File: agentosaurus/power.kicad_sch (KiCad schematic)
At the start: 4 parts, among them J1 ATX_24Pin, U1 TPS54360DDA, U2 AMS1117-3.3

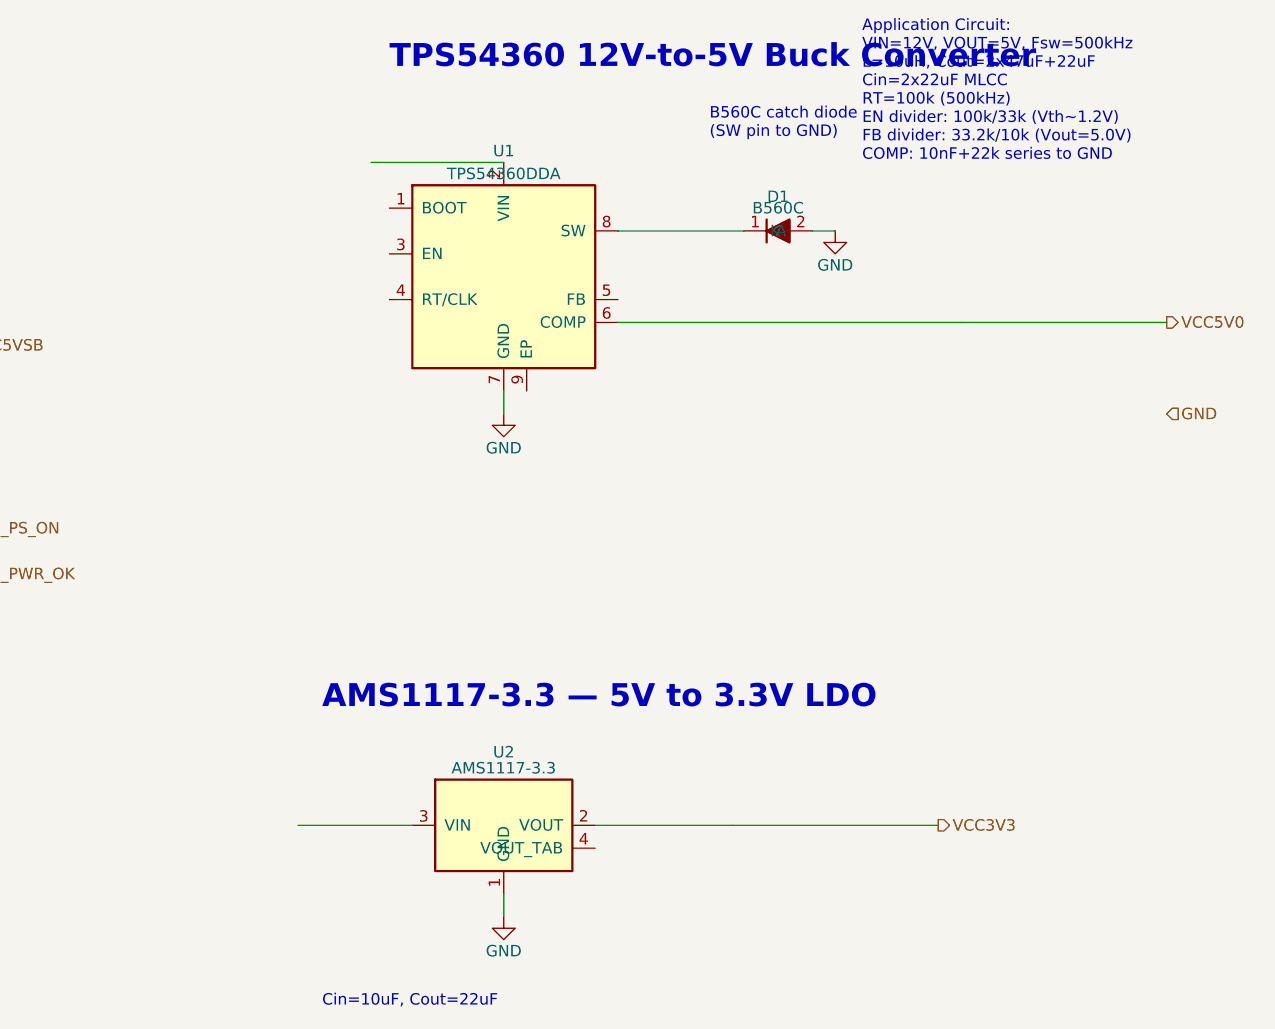
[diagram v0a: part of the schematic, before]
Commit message: Add passive components to all schematic sheets
- power.kicad_sch: Fix D1 catch diode rotation (cathode→SW), remove
  incorrect COMP-to-output wire, add all TPS54360 application circuit
  passives (CIN1/2, CBOOT, L1, COUT1-3, R_EN1/2, R_RT, R_FB1/2,
  R_COMP, C_COMP) and AMS1117 caps (CIN_LDO, COUT_LDO)
- bmc.kicad_sch: Add USB-C CC pull-downs (R1/R2 5.1k), ESP32 reset
  circuit (R3 10k + C9 1uF), decoupling caps for ESP32 (C10/C11),
  UART mux (C12), USB mux (C13/C14), WS2812B (C15-C18), I2C
  pull-ups (R4/R5 4.7k)
- cm4-slot.kicad_sch: Add magnetics center-tap decoupling (C1-C4
  100nF) and power rail decoupling (C5-C8)
- ethernet-switch.kicad_sch: Add crystal load caps (C1/C2 22pF),
  3.3V decoupling (C3-C10), 1.0V core decoupling (C11-C16),
  Slot 2 Ethernet wiring to RTL8367S
- mechanical.kicad_sch: Add PCB stackup, impedance control, and
  via specifications

https://claude.ai/code/session_01UhhXLgEHsAy83XEALyNrDb
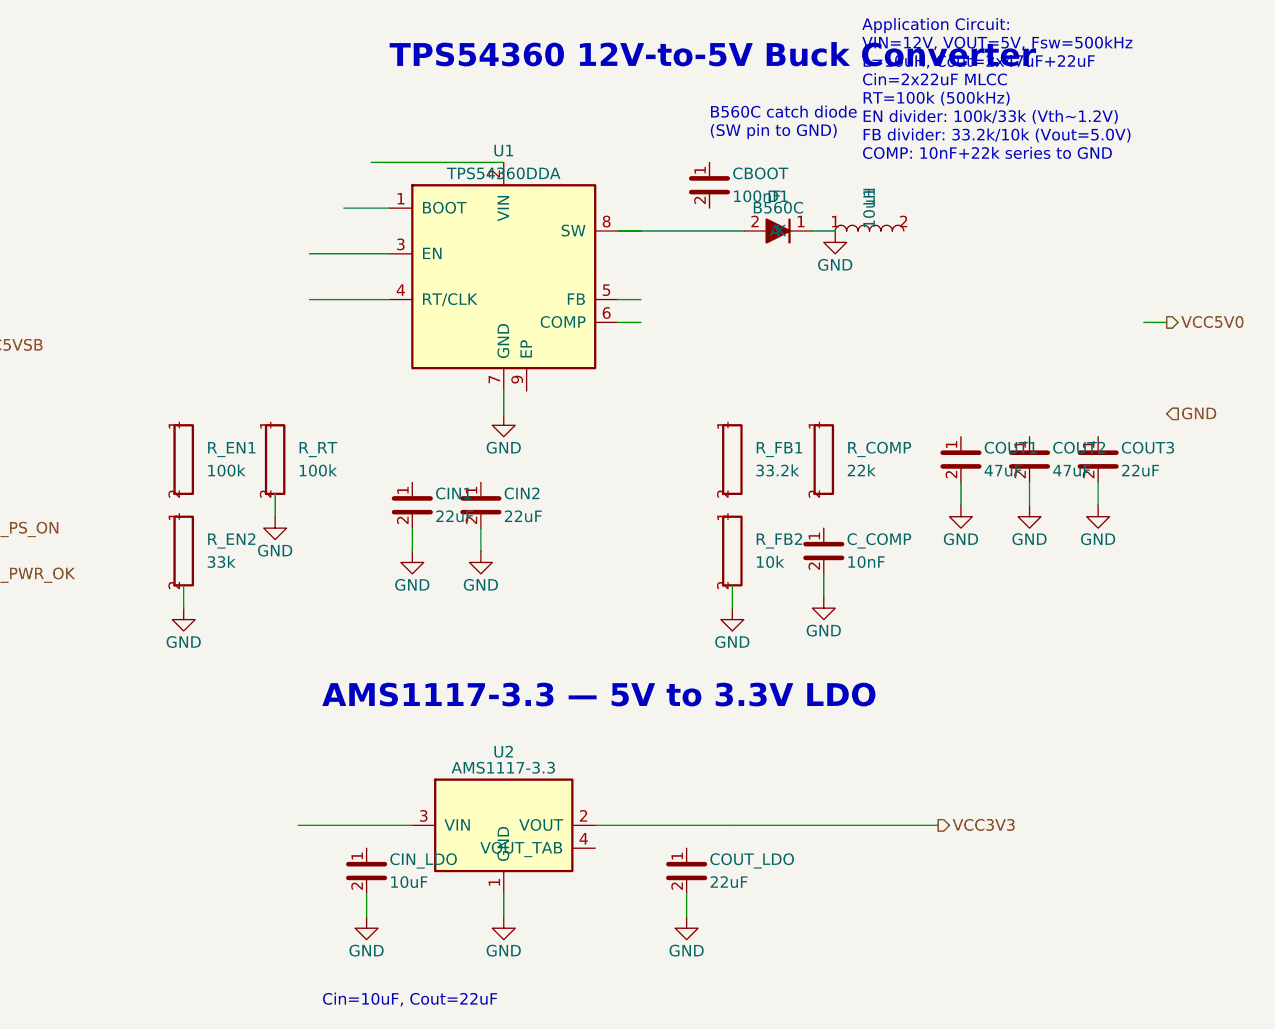
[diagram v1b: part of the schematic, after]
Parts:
- added CBOOT: 100nF, Capacitor_SMD:C_0402_1005Metric, symbol Device:C
- added CIN1, CIN2, COUT3, COUT_LDO: 22uF, Capacitor_SMD:C_0805_2012Metric, symbol Device:C
- added CIN_LDO: 10uF, Capacitor_SMD:C_0805_2012Metric, symbol Device:C
- added COUT1, COUT2: 47uF, Capacitor_SMD:C_0805_2012Metric, symbol Device:C
- added C_COMP: 10nF, Capacitor_SMD:C_0402_1005Metric, symbol Device:C
- added L1: 10uH, Inductor_SMD:L_1210_3225Metric, symbol Device:L
- added R_COMP: 22k, Resistor_SMD:R_0402_1005Metric, symbol Device:R
- added R_EN1, R_RT: 100k, Resistor_SMD:R_0402_1005Metric, symbol Device:R
- added R_EN2: 33k, Resistor_SMD:R_0402_1005Metric, symbol Device:R
- added R_FB1: 33.2k, Resistor_SMD:R_0402_1005Metric, symbol Device:R
- added R_FB2: 10k, Resistor_SMD:R_0402_1005Metric, symbol Device:R
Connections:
- net GND: now also D1.1 (A), CIN1.2, CIN2.2, CIN_LDO.2, COUT1.2, COUT2.2, COUT3.2, COUT_LDO.2, C_COMP.2, L1.1, R_EN2.2, R_FB2.2, R_RT.2; no longer D1.2 (K)
- net VCC5V0: no longer U1.6 (COMP)
- net at U1.8 (SW): now also D1.2 (K); no longer D1.1 (A)
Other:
- moved on the sheet: D1

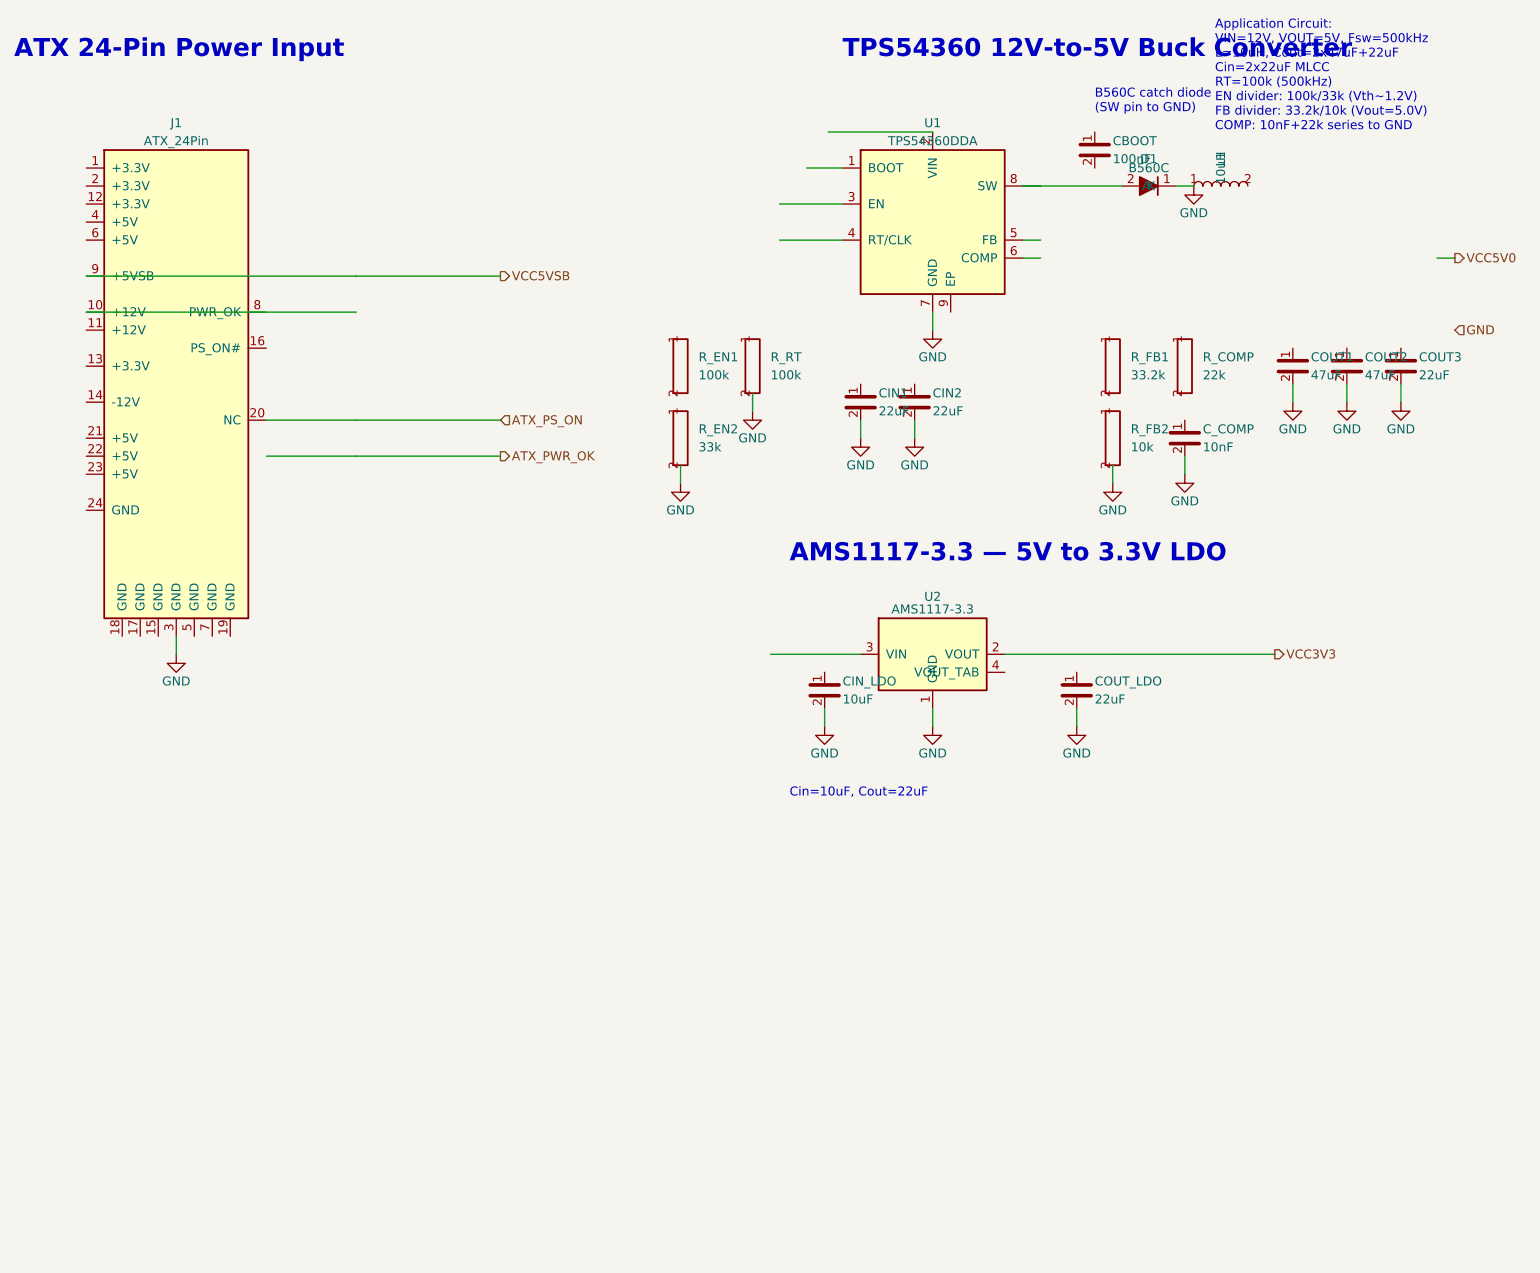
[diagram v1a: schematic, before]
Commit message: Clean up power sheet: reorganize passives and fix net labels
Linter-driven cleanup of power.kicad_sch:
- Simplify reference designators (CIN1→C1, CBOOT→C3, R_EN1→R1, etc.)
- Use cleaner net names (SW, BOOT, EN, FB, COMP, RT_CLK)
- Restore VCC5V0 wire to hierarchical label
- Add EP (exposed pad) to GND connection
- Add GND symbol for hierarchical GND label
- Reorganize passive components into dedicated area below main circuit
- Remove duplicate/redundant net labels and wires

https://claude.ai/code/session_01UhhXLgEHsAy83XEALyNrDb
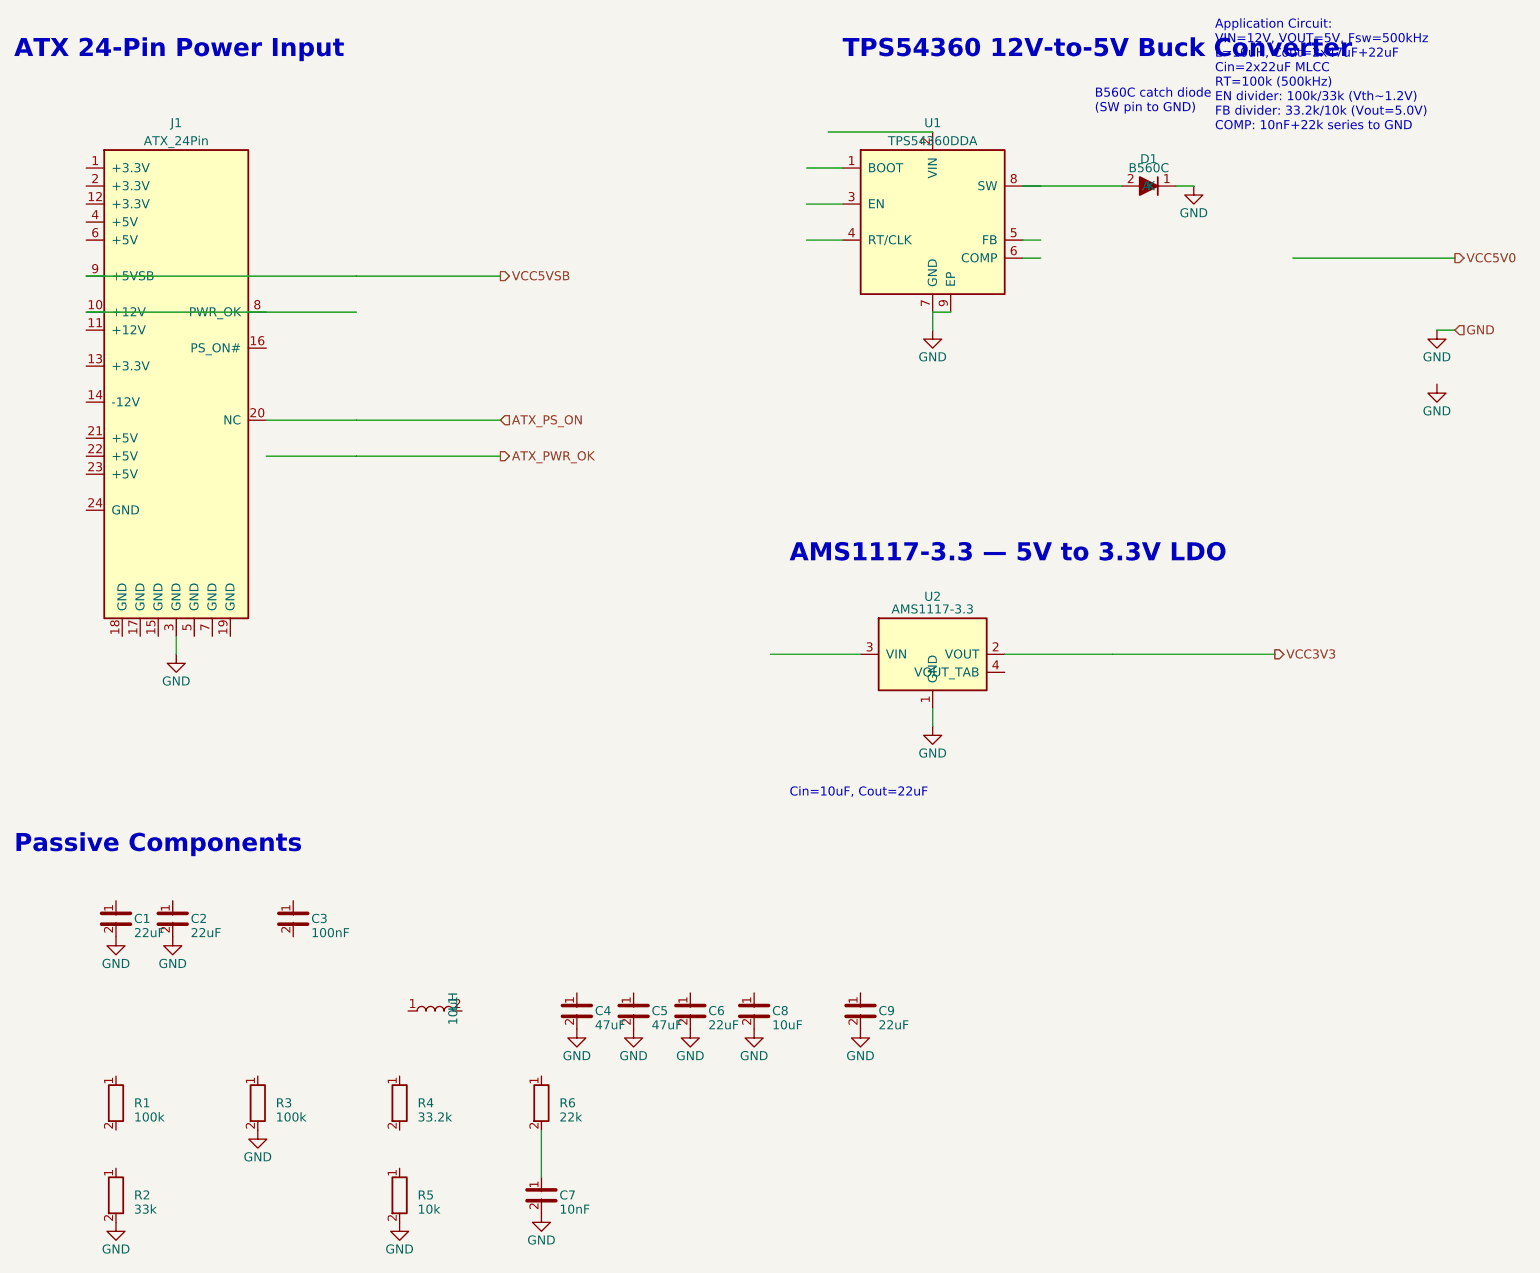
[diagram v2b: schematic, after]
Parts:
- removed CBOOT: 100nF, Capacitor_SMD:C_0402_1005Metric, symbol Device:C
- removed CIN1, CIN2, COUT3, COUT_LDO: 22uF, Capacitor_SMD:C_0805_2012Metric, symbol Device:C
- removed CIN_LDO: 10uF, Capacitor_SMD:C_0805_2012Metric, symbol Device:C
- removed COUT1, COUT2: 47uF, Capacitor_SMD:C_0805_2012Metric, symbol Device:C
- removed C_COMP: 10nF, Capacitor_SMD:C_0402_1005Metric, symbol Device:C
- removed R_COMP: 22k, Resistor_SMD:R_0402_1005Metric, symbol Device:R
- removed R_EN1, R_RT: 100k, Resistor_SMD:R_0402_1005Metric, symbol Device:R
- removed R_EN2: 33k, Resistor_SMD:R_0402_1005Metric, symbol Device:R
- removed R_FB1: 33.2k, Resistor_SMD:R_0402_1005Metric, symbol Device:R
- removed R_FB2: 10k, Resistor_SMD:R_0402_1005Metric, symbol Device:R
- added C1, C2, C6, C9: 22uF, Capacitor_SMD:C_0805_2012Metric, symbol Device:C
- added C3: 100nF, Capacitor_SMD:C_0402_1005Metric, symbol Device:C
- added C4, C5: 47uF, Capacitor_SMD:C_1206_3216Metric, symbol Device:C
- added C7: 10nF, Capacitor_SMD:C_0402_1005Metric, symbol Device:C
- added C8: 10uF, Capacitor_SMD:C_0805_2012Metric, symbol Device:C
- added R1, R3: 100k, Resistor_SMD:R_0402_1005Metric, symbol Device:R
- added R2: 33k, Resistor_SMD:R_0402_1005Metric, symbol Device:R
- added R4: 33.2k, Resistor_SMD:R_0402_1005Metric, symbol Device:R
- added R5: 10k, Resistor_SMD:R_0402_1005Metric, symbol Device:R
- added R6: 22k, Resistor_SMD:R_0402_1005Metric, symbol Device:R
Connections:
- net GND: now also U1.9 (EP), C1.2, C2.2, C4.2, C5.2, C6.2, C7.2, C8.2, C9.2, R2.2, R3.2, R5.2; no longer L1.1
- new net: C7.1, R6.2
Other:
- note added: "Passive Components"
